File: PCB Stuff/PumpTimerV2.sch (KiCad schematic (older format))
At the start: 30 parts, among them J1 282856-2, J2 282856-2, J3 282856-2, J4 Conn_02x20_Odd_Even, J6 B4B-PH-SM4-TBT(LF)(SN), K1 ADW1205HLW, K2 ADW1205HLW, Q1 DMN67D7L, Q2 DMN67D7L, SW1 TL3305AF160QG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

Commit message: Potentially final routing & review. Might check things over one more time before submitting for fab
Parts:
- added C3: 100u, Capacitor_SMD:C_1206_3216Metric_Pad1.33x1.80mm_HandSolder, symbol Device:C
- added D3: BAV5004WS-7, Diode_SMD:D_SOD-323, symbol Simulation_SPICE:DIODE
- added R5: 2k2, Resistor_SMD:R_0603_1608Metric_Pad0.98x0.95mm_HandSolder, symbol Device:R_US
- C1, C2: Part (none) -> GMC31X5R107M10NT
- R1, R2: value 1k -> 10k; Part (none) -> ERJ-PA3J103V
- renumbered D3 to D2
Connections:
- net +3V3: now also R5.1
- net +5VD: now also C3.1
- net +BATT: now also D3.2 (K); no longer BT1.POS (+)
- net GND: now also C3.2
- net RLY_R: now also J4.8 (Pin_8), Q1.1 (G), R1.2; no longer J4.12 (Pin_12), Q2.1 (G), R2.2
- net RLY_S: now also J4.12 (Pin_12), Q2.1 (G), R2.2; no longer J4.8 (Pin_8), Q1.1 (G), R1.2
- net RTC_~INT~: now also R5.2
- net Reset: now also D1.1 (A), K1.1, K2.1, Q1.3 (D); no longer D2.1 (A), K1.6, K2.6, Q2.3 (D)
- net Set: now also D2.1 (A), K1.6, K2.6, Q2.3 (D); no longer D1.1 (A), K1.1, K2.1, Q1.3 (D)
- net GPIO4: now reaches J4.7 (Pin_7)
- net GPIO4: now also R13.2, SW1.1
- new net: BT1.POS (+), D3.1 (A)
- no-connect marks 28 -> 27
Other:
- moved on the sheet: BT1, R13, SW1

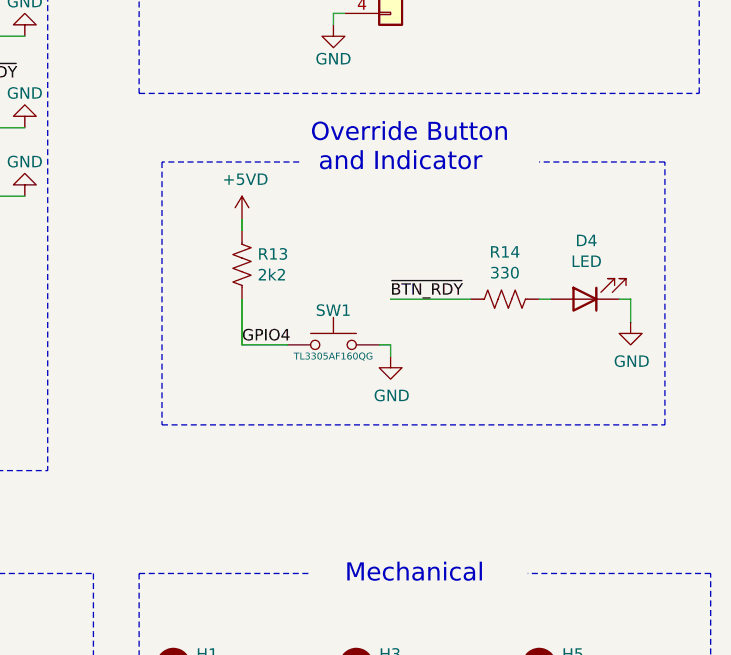
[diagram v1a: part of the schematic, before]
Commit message: Finished routing bigger AC-line traces
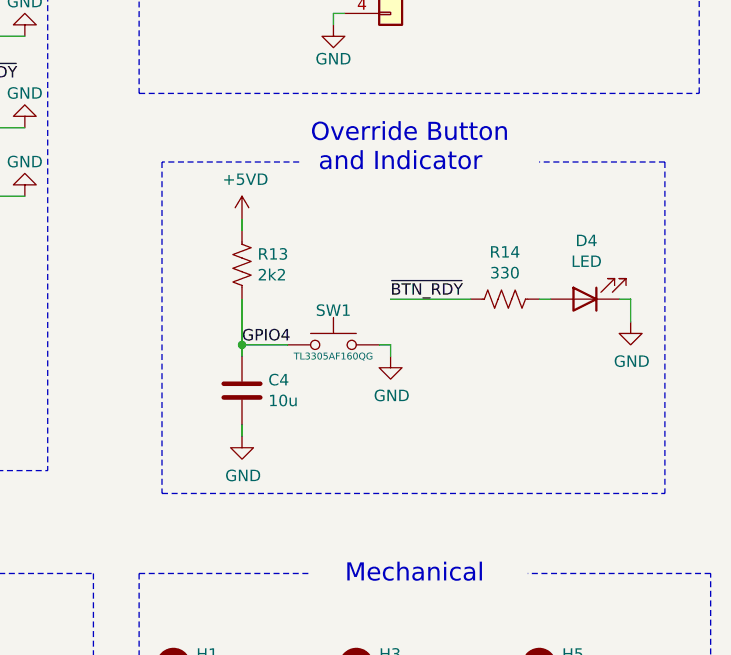
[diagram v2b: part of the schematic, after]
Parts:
- added C4: 10u, Capacitor_SMD:C_0603_1608Metric_Pad1.08x0.95mm_HandSolder, symbol Device:C
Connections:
- net GND: now also C4.2
- net GPIO4: now also C4.1
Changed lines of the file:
@@
 encoding utf-8
 Sheet 1 1
-Title ""
+Title "PumpTimerV2"
 Date "2021-04-15"
-Rev ""
-Comp ""
+Rev "-"
+Comp "Taylor Zinke"
 Comment1 ""
 Comment2 ""
@@
 Wire Notes Line width 10 style solid
 	9350 2600 8750 2600
-Wire Notes Line width 10 style solid
-	8750 2600 8750 3750
-Wire Notes Line width 10 style solid
-	8750 3750 10950 3750
-Wire Notes Line width 10 style solid
-	10950 3750 10950 2600
 Text Notes 9400 2650 0    79   ~ 0
 Override Button\n and Indicator
@@
 	1    0    0    -1
 $EndComp
+$Comp
+L Device:C C4
+U 1 1 60875735
+P 9100 3600
+F 0 "C4" H 9215 3646 50  0000 L CNN
+F 1 "10u" H 9215 3555 50  0000 L CNN
+F 2 "Capacitor_SMD:C_0603_1608Metric_Pad1.08x0.95mm_HandSolder" H 9138 3450 50  0001 C CNN
+F 3 "~" H 9100 3600 50  0001 C CNN
+F 4 "Something that's like 10u" H 9100 3600 50  0001 C CNN "Part"
+	1    9100 3600
+	1    0    0    -1
+$EndComp
+Wire Wire Line
+	9100 3450 9100 3400
+Connection ~ 9100 3400
+$Comp
+L power:GND #PWR031
+U 1 1 60878A93
+P 9100 3800
+F 0 "#PWR031" H 9100 3550 50  0001 C CNN
+F 1 "GND" H 9105 3627 50  0000 C CNN
+F 2 "" H 9100 3800 50  0001 C CNN
+F 3 "" H 9100 3800 50  0001 C CNN
+	1    9100 3800
+	1    0    0    -1
+$EndComp
+Wire Wire Line
+	9100 3750 9100 3800
+Wire Notes Line width 10 style solid
+	8750 4050 10950 4050
+Wire Notes Line width 10 style solid
+	8750 2600 8750 4050
+Wire Notes Line width 10 style solid
+	10950 2600 10950 4050
 $EndSCHEMATC

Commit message: Adding BOM
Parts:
- C4: Part Something that's like 10u -> LMK107BJ106MALTD
- D1, D2, D3: Part (none) -> BAV5004WS-7
- J1, J2, J3: Comment 282856-2 -> (none); Part (none) -> 282856-2
- J6: Part (none) -> B4B-PH-SM4-TBT(LF)(SN)
- K1, K2: Part (none) -> ADW1205HLW
- PS1: MP RAC03-05SK -> (none); Part (none) -> RAC03-05SK
- Q1, Q2: Part (none) -> DMN67D7L
- R3, R4, R5: Part (none) -> CRGP0603F2K2
- U1: Part (none) -> RX8900UA
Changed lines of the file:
@@
 F 5 "None" H 1850 1950 50  0001 L BNN "Package"
 F 6 "Unavailable" H 1850 1950 50  0001 L BNN "Availability"
-F 7 "RAC03-05SK" H 1850 1950 50  0001 L BNN "MP"
+F 7 "RAC03-05SK" H 1850 1950 50  0001 L BNN "Part"
 F 8 "None" H 1850 1950 50  0001 L BNN "Price"
 F 9 "Recom Power" H 1850 1950 50  0001 L BNN "MF"
@@
 F 4 "Manufacturer Recommendation" H 1700 5950 50  0001 L BNN "STANDARD"
 F 5 "Panasonic" H 1700 5950 50  0001 L BNN "MANUFACTURER"
+F 6 "ADW1205HLW" H 1700 5950 50  0001 C CNN "Part"
 	1    1700 5950
 	1    0    0    -1
@@
 F 4 "Manufacturer Recommendation" H 3850 5950 50  0001 L BNN "STANDARD"
 F 5 "Panasonic" H 3850 5950 50  0001 L BNN "MANUFACTURER"
+F 6 "ADW1205HLW" H 3850 5950 50  0001 C CNN "Part"
 	1    3850 5950
 	1    0    0    -1
@@
 F 2 "Package_TO_SOT_SMD:SOT-23" H 2100 6625 50  0001 L CIN
 F 3 "http://www.diodes.com/assets/Datasheets/DMN67D7L.pdf" H 1900 6700 50  0001 L CNN
+F 4 "DMN67D7L" H 1900 6700 50  0001 C CNN "Part"
 	1    1900 6700
 	1    0    0    -1
@@
 F 2 "Package_TO_SOT_SMD:SOT-23" H 3650 6625 50  0001 L CIN
 F 3 "http://www.diodes.com/assets/Datasheets/DMN67D7L.pdf" H 3450 6700 50  0001 L CNN
+F 4 "DMN67D7L" H 3450 6700 50  0001 C CNN "Part"
 	1    3450 6700
 	1    0    0    -1
@@
 F 4 "Y" H 2150 4950 50  0001 L CNN "Spice_Netlist_Enabled"
 F 5 "D" H 2150 4950 50  0001 L CNN "Spice_Primitive"
+F 6 "BAV5004WS-7" V 2150 4950 50  0001 C CNN "Part"
 	1    2150 4950
 	0    -1   -1   0
@@
 F 4 "Y" H 3000 4950 50  0001 L CNN "Spice_Netlist_Enabled"
 F 5 "D" H 3000 4950 50  0001 L CNN "Spice_Primitive"
+F 6 "BAV5004WS-7" V 3000 4950 50  0001 C CNN "Part"
 	1    3000 4950
 	0    -1   -1   0
@@
 F 2 "Package_SO:SOP-14_127P780x200" H 6000 4000 50  0001 C CNN
 F 3 "" H 6000 4000 50  0001 C CNN
+F 4 "RX8900UA" H 5900 4850 50  0001 C CNN "Part"
 	1    5900 4850
 	1    0    0    -1
@@
 F 2 "Resistor_SMD:R_0603_1608Metric_Pad0.98x0.95mm_HandSolder" V 5790 1740 50  0001 C CNN
 F 3 "CRGP0603F2K2" H 5750 1750 50  0001 C CNN
+F 4 "CRGP0603F2K2" H 5750 1750 50  0001 C CNN "Part"
 	1    5750 1750
 	1    0    0    -1
@@
 F 3 "" H 4250 2400 50  0001 L BNN
 F 4 "Compliant with Exemptions" H 4250 2400 50  0001 L BNN "EU_RoHS_Compliance"
-F 5 "282856-2" H 4250 2400 50  0001 L BNN "Comment"
+F 5 "282856-2" H 4250 2400 50  0001 L BNN "Part"
 	1    4250 2400
 	1    0    0    -1
@@
 F 2 "Resistor_SMD:R_0603_1608Metric_Pad0.98x0.95mm_HandSolder" V 6090 1740 50  0001 C CNN
 F 3 "CRGP0603F2K2" H 6050 1750 50  0001 C CNN
+F 4 "CRGP0603F2K2" H 6050 1750 50  0001 C CNN "Part"
 	1    6050 1750
 	1    0    0    -1
@@
 F 2 "Connector_JST:JST_PH_B4B-PH-SM4-TB_1x04-1MP_P2.00mm_Vertical" H 9750 1750 50  0001 C CNN
 F 3 "~" H 9750 1750 50  0001 C CNN
+F 4 "B4B-PH-SM4-TBT(LF)(SN)" H 9750 1750 50  0001 C CNN "Part"
 	1    9750 1750
 	1    0    0    -1
@@
 F 3 "" H 4250 1850 50  0001 L BNN
 F 4 "Compliant with Exemptions" H 4250 1850 50  0001 L BNN "EU_RoHS_Compliance"
-F 5 "282856-2" H 4250 1850 50  0001 L BNN "Comment"
+F 5 "282856-2" H 4250 1850 50  0001 L BNN "Part"
 	1    4250 1850
 	1    0    0    -1
@@
 F 3 "" H 4250 2950 50  0001 L BNN
 F 4 "Compliant with Exemptions" H 4250 2950 50  0001 L BNN "EU_RoHS_Compliance"
-F 5 "282856-2" H 4250 2950 50  0001 L BNN "Comment"
+F 5 "282856-2" H 4250 2950 50  0001 L BNN "Part"
 	1    4250 2950
 	1    0    0    -1
@@
 F 4 "Y" H 7600 5000 50  0001 L CNN "Spice_Netlist_Enabled"
 F 5 "D" H 7600 5000 50  0001 L CNN "Spice_Primitive"
+F 6 "BAV5004WS-7" V 7600 5000 50  0001 C CNN "Part"
 	1    7600 5000
 	0    -1   -1   0
@@
 F 2 "Resistor_SMD:R_0603_1608Metric_Pad0.98x0.95mm_HandSolder" V 7240 5090 50  0001 C CNN
 F 3 "CRGP0603F2K2" H 7200 5100 50  0001 C CNN
+F 4 "CRGP0603F2K2" H 7200 5100 50  0001 C CNN "Part"
 	1    7200 5100
 	1    0    0    -1
@@
 F 2 "Capacitor_SMD:C_0603_1608Metric_Pad1.08x0.95mm_HandSolder" H 9138 3450 50  0001 C CNN
 F 3 "~" H 9100 3600 50  0001 C CNN
-F 4 "Something that's like 10u" H 9100 3600 50  0001 C CNN "Part"
+F 4 "LMK107BJ106MALTD" H 9100 3600 50  0001 C CNN "Part"
 	1    9100 3600
 	1    0    0    -1

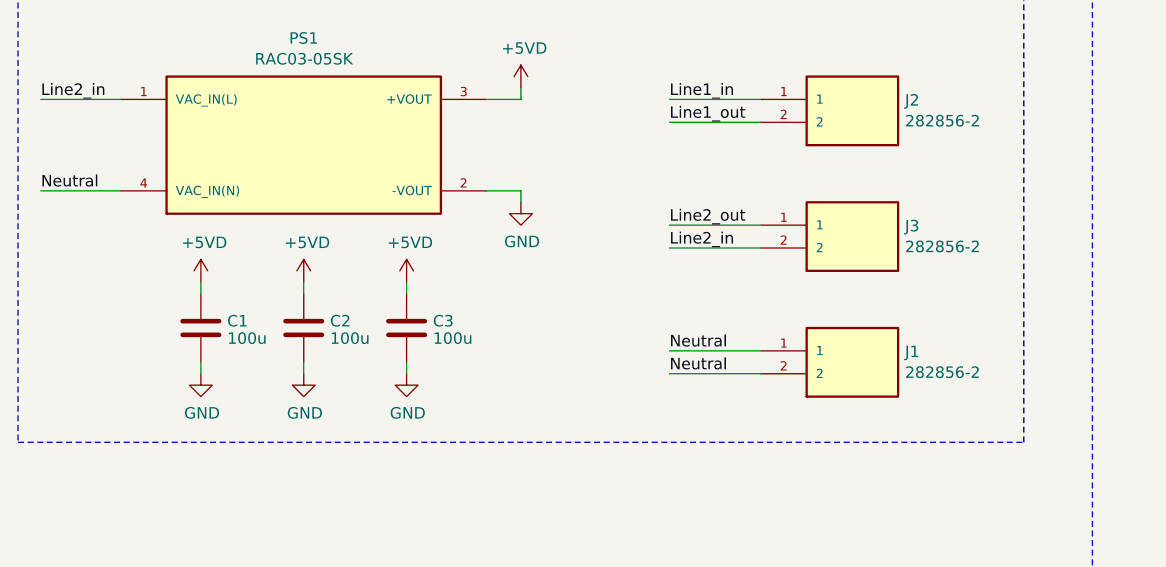
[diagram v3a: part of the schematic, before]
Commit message: Removed "Neutral" net (my AC/DC converter died. Seems like 230V input is nominal anyways)
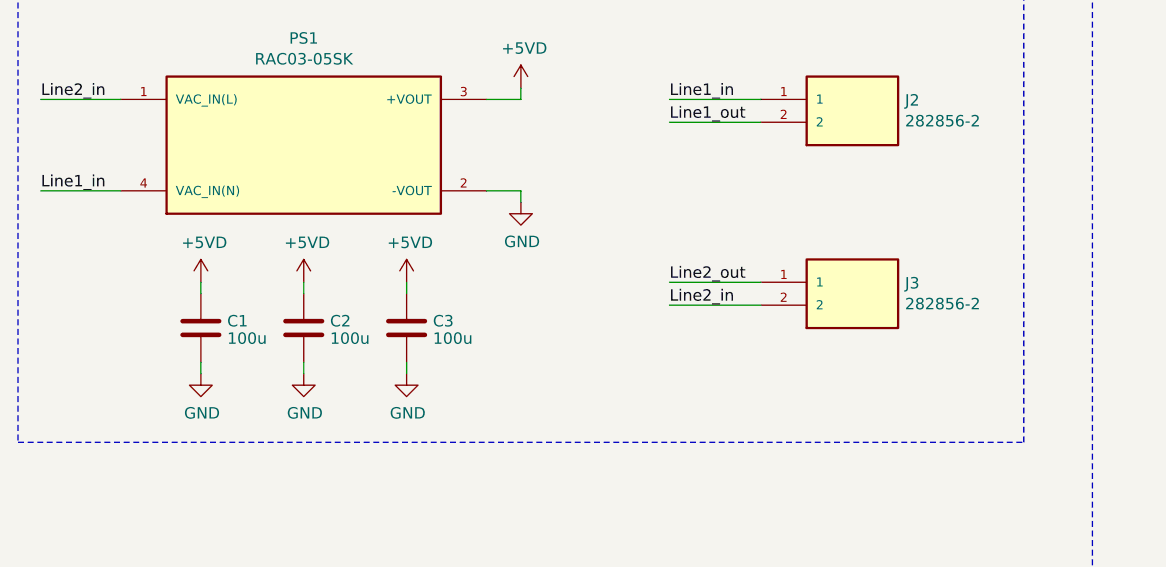
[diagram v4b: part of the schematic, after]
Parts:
- removed J1: 282856-2, TE_282856-2, symbol Connector:282856-2
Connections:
- net Neutral is gone; now on net Line1_in: PS1.4 (VAC_IN(N))
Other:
- moved on the sheet: J3
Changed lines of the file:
@@
 Line2_in
 Text Label 700  2150 0    50   ~ 0
-Neutral
+Line1_in
 Wire Wire Line
 	700  2150 1050 2150
@@
 	8250 1200 7700 1200
 Wire Wire Line
-	3850 2950 3450 2950
-Wire Wire Line
-	3450 2850 3850 2850
-Wire Wire Line
-	3850 2400 3450 2400
-Wire Wire Line
-	3450 2300 3850 2300
-Text Label 3450 2950 0    50   ~ 0
-Neutral
-Text Label 3450 2850 0    50   ~ 0
-Neutral
-Text Label 3450 2300 0    50   ~ 0
+	3850 2650 3450 2650
+Wire Wire Line
+	3450 2550 3850 2550
+Text Label 3450 2550 0    50   ~ 0
 Line2_out
-Text Label 3450 2400 0    50   ~ 0
+Text Label 3450 2650 0    50   ~ 0
 Line2_in
 Wire Wire Line
@@
 L Connector:282856-2 J3
 U 1 1 6074D2DA
-P 4250 2400
-F 0 "J3" H 4480 2496 50  0000 L CNN
-F 1 "282856-2" H 4480 2405 50  0000 L CNN
-F 2 "TE_282856-2" H 4250 2400 50  0001 L BNN
-F 3 "" H 4250 2400 50  0001 L BNN
-F 4 "Compliant with Exemptions" H 4250 2400 50  0001 L BNN "EU_RoHS_Compliance"
-F 5 "282856-2" H 4250 2400 50  0001 L BNN "Part"
-	1    4250 2400
+P 4250 2650
+F 0 "J3" H 4480 2746 50  0000 L CNN
+F 1 "282856-2" H 4480 2655 50  0000 L CNN
+F 2 "TE_282856-2" H 4250 2650 50  0001 L BNN
+F 3 "" H 4250 2650 50  0001 L BNN
+F 4 "Compliant with Exemptions" H 4250 2650 50  0001 L BNN "EU_RoHS_Compliance"
+F 5 "282856-2" H 4250 2650 50  0001 L BNN "Part"
+	1    4250 2650
 	1    0    0    -1
 $EndComp
@@
 	1    0    0    -1
 $EndComp
-$Comp
-L Connector:282856-2 J1
-U 1 1 6083B1AC
-P 4250 2950
-F 0 "J1" H 4480 3046 50  0000 L CNN
-F 1 "282856-2" H 4480 2955 50  0000 L CNN
-F 2 "TE_282856-2" H 4250 2950 50  0001 L BNN
-F 3 "" H 4250 2950 50  0001 L BNN
-F 4 "Compliant with Exemptions" H 4250 2950 50  0001 L BNN "EU_RoHS_Compliance"
-F 5 "282856-2" H 4250 2950 50  0001 L BNN "Part"
-	1    4250 2950
-	1    0    0    -1
-$EndComp
